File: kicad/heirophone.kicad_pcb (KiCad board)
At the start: 2 copper layers, 220 x 130 mm, 158 parts, among them J1 AudioJack2_SwitchT, J10 Conn_01x02, J2 AudioJack2_SwitchT, J3 Conn_01x03_Pin, J4 AudioJack2_SwitchT, J5 AudioJack2_SwitchT, J6 AudioJack2_SwitchT, J7 AudioJack2_SwitchT, J8 Conn_01x02, J9 Conn_01x02, Q1 2N3904, Q2 2N3906, Q3 2N3906, SW1 SW_SPDT, SW2 SW_SPDT, SW3 SW_SPDT, U10 TL072, U11 TL072, U12 TL072, U13 TL072, U2 LM13700, U3 LM13700, U4 TL072, U5 TL072, U6 LM386, U7 NE5534, U8 TL072, U9 ICL7660

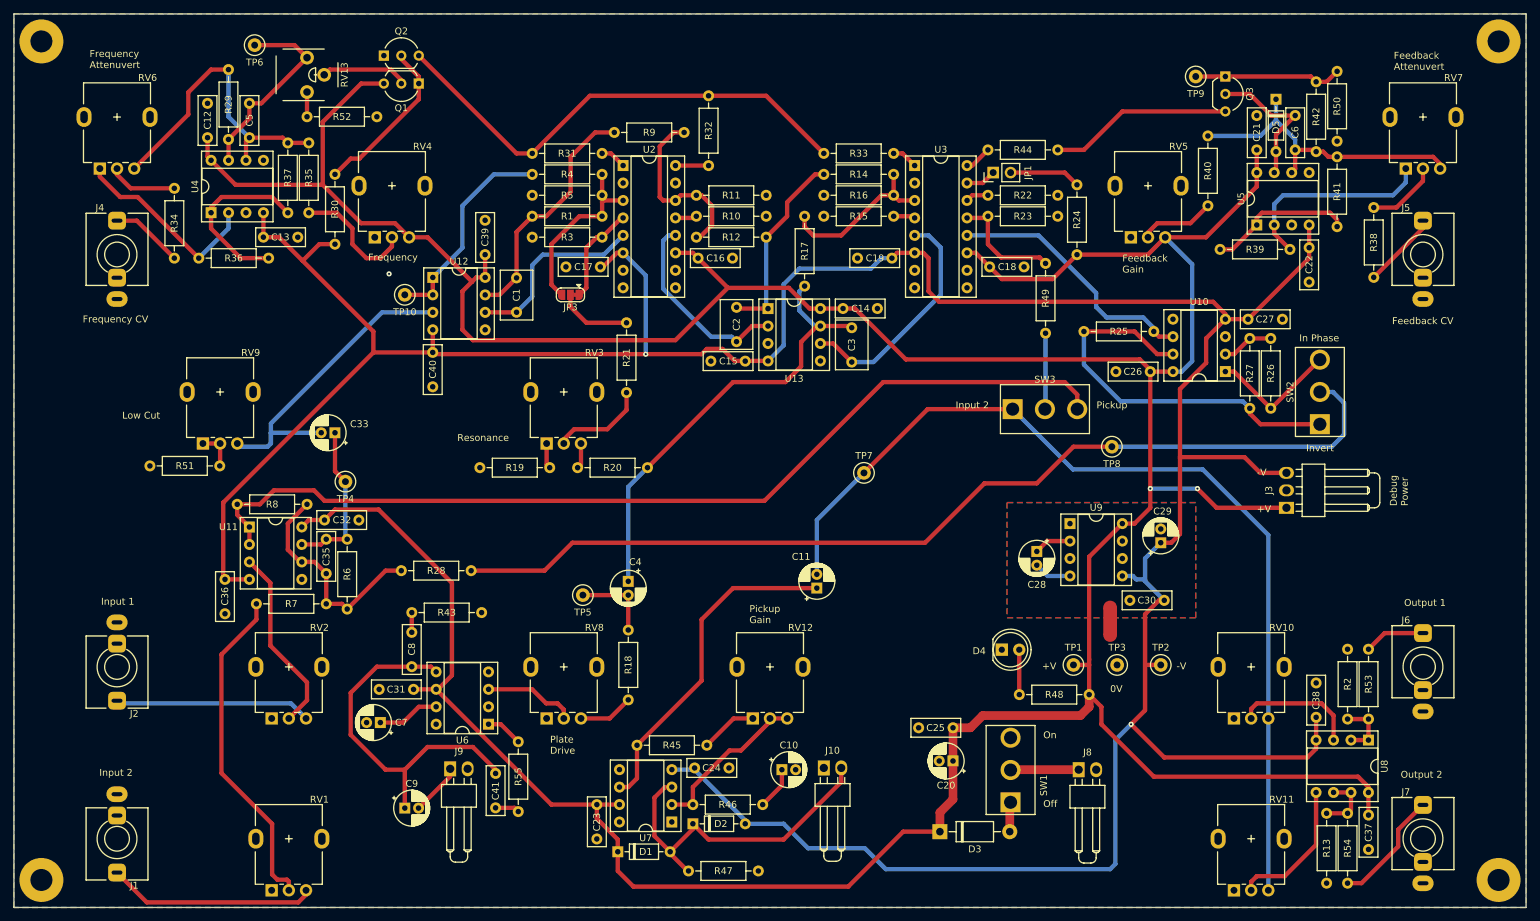
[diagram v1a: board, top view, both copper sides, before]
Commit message: Redesign feedback VCA to be a multiplier
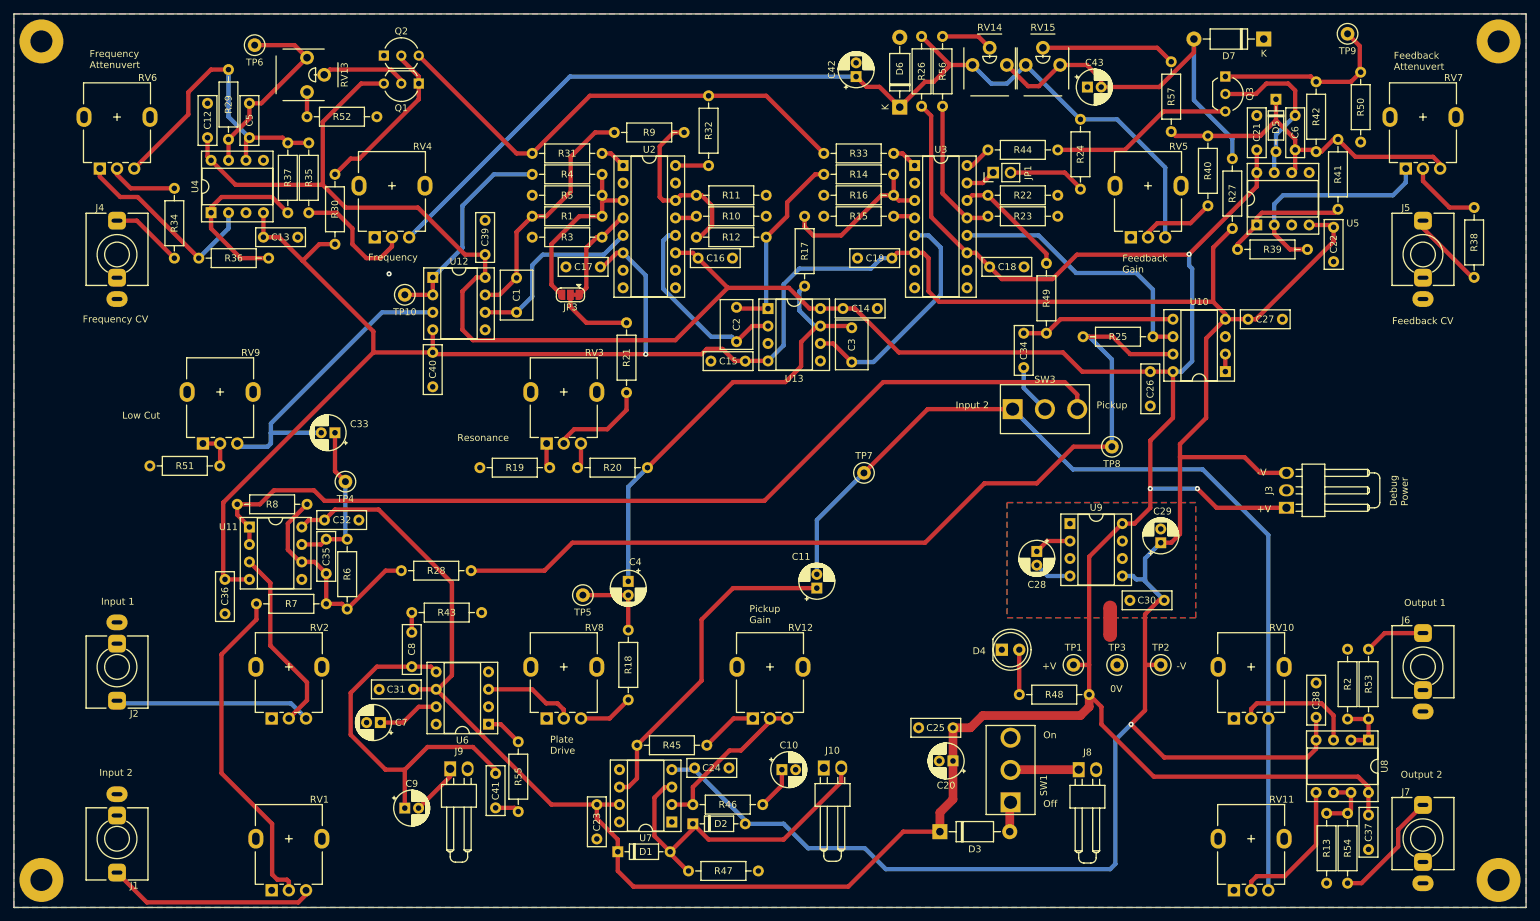
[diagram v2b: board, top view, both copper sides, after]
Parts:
- removed SW2: SW_SPDT, Rumblesan_Standard_Parts:Toggle_Switch_100SP-M2
- added C34: 100nF, Rumblesan_Standard_Parts:C_Rect_L7.0mm_W2.5mm_P5.00mm, F.Cu at (176.9, 76.5)
- added C42: 10uF, Rumblesan_Standard_Parts:CP_Radial_D5.0mm_P2.00mm, F.Cu at (152.5, 39.1)
- added C43: 10uF, Rumblesan_Standard_Parts:CP_Radial_D5.0mm_P2.00mm, F.Cu at (186.2, 40.6)
- added D6: 5v1, Diode_THT:D_DO-41_SOD81_P10.16mm_Horizontal, F.Cu at (158.9, 43.6)
- added D7: 5v1, Diode_THT:D_DO-41_SOD81_P10.16mm_Horizontal, F.Cu at (211.8, 33.7)
- added R56: 100k, Rumblesan_Standard_Parts:R_Axial_DIN0207_L6.3mm_D2.5mm_P10.16mm_Horizontal, F.Cu at (165.1, 33.3)
- added R57: 100k, Rumblesan_Standard_Parts:R_Axial_DIN0207_L6.3mm_D2.5mm_P10.16mm_Horizontal, F.Cu at (198.4, 37.0)
- added RV14: 100k, Rumblesan_Potentiometer_THT:Potentiometer_THT_Bourns_3306P_Vertical, F.Cu at (172.0, 36.2)
- added RV15: 100k, Rumblesan_Potentiometer_THT:Potentiometer_THT_Bourns_3306P_Vertical, F.Cu at (179.7, 36.2)
- R26, R27: value 10k -> 1k
- moved R26 61.0 mm to (162.1, 43.4), turned to 90 degrees
- moved R27 26.3 mm to (207.3, 61.2)
- moved TP9 22.9 mm to (224.0, 32.9)
- moved R38 14.6 mm to (242.4, 68.3)
- moved C22 4.63 mm to (222.0, 66.0)
- moved R50 3.43 mm to (225.9, 38.5)
- moved R39 2.54 mm to (218.2, 64.3)
- moved R41 2.53 mm to (222.6, 58.4)
- moved R24 0.81 mm to (185.2, 55.5), turned to 90 degrees
- moved R25 0.77 mm to (195.7, 77.0)
- moved R49 0.13 mm to (180.2, 76.5)
- turned C26 to -90 degrees
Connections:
- R24 pad 2: VCC -> /POS_5V_REF
- R25 pad 2: Net-(SW2-A) -> Net-(R25-Pad2)
- R26 pad 1: Net-(U10A--) -> VCC
- R26 pad 2: Net-(SW2-C) -> /POS_5V_REF
- R27 pad 1: Net-(SW2-A) -> VEE
- R27 pad 2: Net-(U10A--) -> /NEG_5V_REF
- R28 pad 2: Net-(SW2-B) -> Net-(R25-Pad2)
- R49 pad 1: Net-(SW3-B) -> Net-(U10B-+)
- R49 pad 2: Net-(U3A--) -> Net-(U3A-+)
- RV4 pad 3: VCC -> /POS_5V_REF
- RV5 pad 3: VCC -> /POS_5V_REF
- TP8 pad 1: Net-(SW2-B) -> Net-(R25-Pad2)
- U10 pad 1: Net-(SW2-C) -> Net-(U10A--)
- U10 pad 3: GND -> unconnected-(U10A-+-Pad3)
- U10 pad 5: GND -> Net-(U10B-+)
- U10 pad 7: Net-(SW2-A) -> Net-(R25-Pad2)
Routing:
- net /POS_5V_REF: track 0.00 -> 148.6 mm
- net Net-(SW2-B): track 144.0 -> 0.00 mm
- net Net-(R25-Pad2): track 0.00 -> 133.1 mm
- net Net-(SW2-A): track 57.5 -> 0.00 mm
- net /NEG_5V_REF: track 0.00 -> 55.5 mm
- net Net-(U10B-+): track 0.00 -> 22.6 mm
- net VCC: track 590.3 -> 612.0 mm, vias 2 -> 3
- net Net-(R57-Pad1): track 0.00 -> 19.5 mm
- net Net-(SW2-C): track 18.9 -> 0.00 mm
- net VEE: track 485.4 -> 502.7 mm
- net Net-(U3A-+): track 3.35 -> 16.8 mm
- net Net-(R56-Pad1): track 0.00 -> 7.54 mm
- net Net-(D5-K): track 45.5 -> 52.6 mm
- net Net-(Q3-E): track 21.5 -> 27.0 mm
- net Net-(U10A--): track 7.55 -> 2.54 mm
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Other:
- board text removed: "In Phase"
- board text removed: "Invert"
